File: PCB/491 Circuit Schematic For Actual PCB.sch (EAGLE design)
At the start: 22 parts, among them J1 DCJ0202, X2 1751248

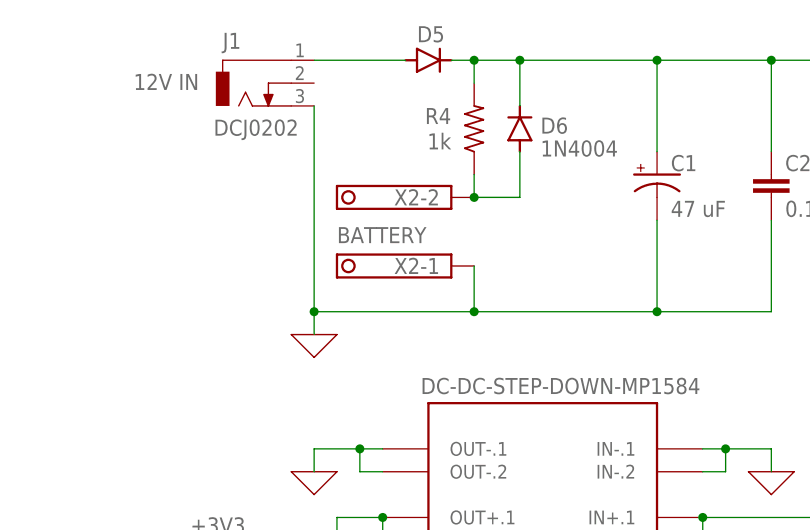
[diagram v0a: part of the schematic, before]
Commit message: JST Battery Connector
Changed battery connector from a screw terminal to a JST connector to make sure it gets plugged in correctly.
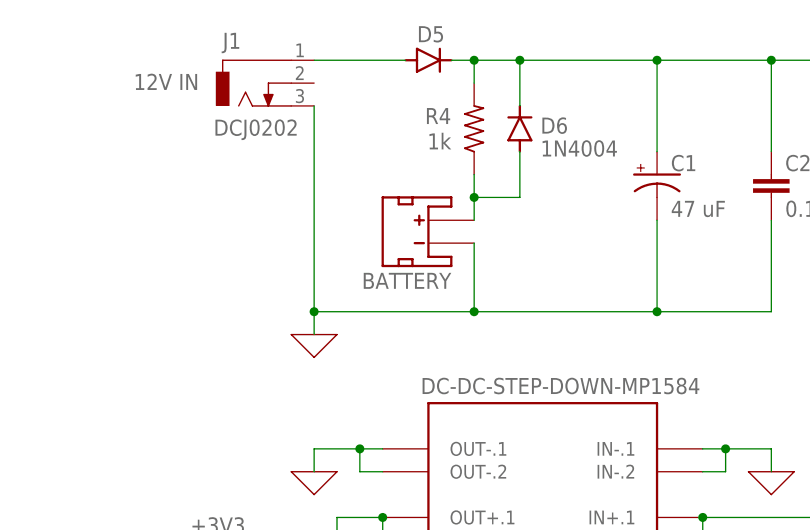
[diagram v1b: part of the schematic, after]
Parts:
- removed X2: 1751248, con-phoenix-350:1751248
- added BATTERY: (no value), cool_safe_lib:JST_2MM_MALE
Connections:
- net 0: now also BATTERY.-; no longer X2-1.K
- net N$1: now also BATTERY.+; no longer X2-2.K
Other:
- note removed: "BATTERY"
